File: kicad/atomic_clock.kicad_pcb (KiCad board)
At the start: 2 copper layers, 282.7 x 43 mm, 88 parts, among them J1 Conn_02x05_Top_Bottom, J10 Conn_02x05_Top_Bottom, J11 Conn_02x05_Top_Bottom, J12 USB_B_Micro 10118194-0001LF, J13 ARM_JTAG_SWD_10 3220-10-0100-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, J14 Conn_01x03_Female, J2 Conn_02x05_Top_Bottom, J3 Conn_02x05_Top_Bottom, J4 Conn_02x05_Top_Bottom, J5 USB_B_Micro 1051330001, J6 Conn_02x05_Top_Bottom, J7 Conn_02x05_Top_Bottom, J8 Conn_02x05_Top_Bottom, J9 Conn_02x05_Top_Bottom, Q1 Q_Dual_PMOS, Q2 Q_Dual_PMOS, SW1 SW_Push, U1 D198K, U10 ATSAMDA1E16B-A, U11 D198K, U12 D198K, U13 D198K, U14 D198K, U15 D198K, U16 MAX7221xWG, U17 D198K, U18 D198K, U19 D198K, U2 D198K, U20 NCP1117LPST33T3G, U21 mems_osc_st1630, U22 DHT20, U23 DCF77, U24 MCP73831-2-OT, U25 TXB0101, U3 D198K, U4 D198K, U5 MAX7221xWG, U6 D198K, U7 D198K, U8 D198K, U9 D198K

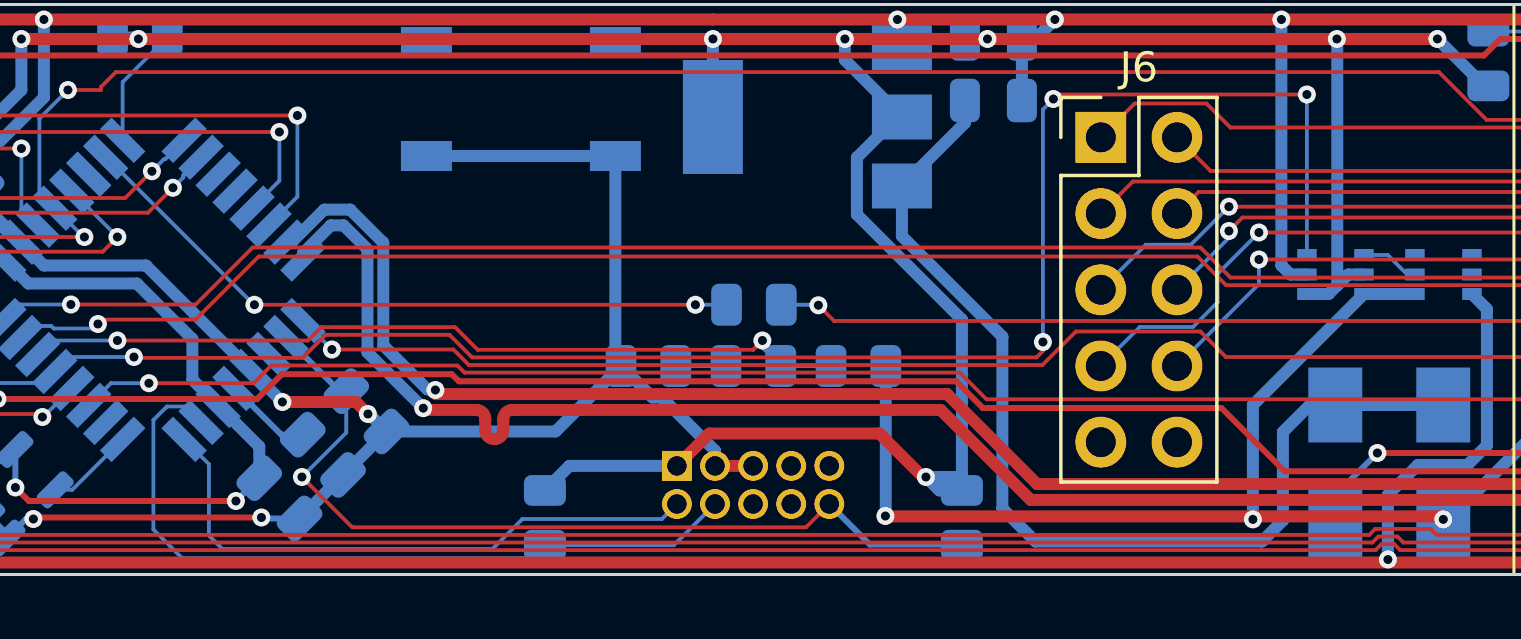
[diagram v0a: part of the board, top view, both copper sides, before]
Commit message: Widen debug connector footprint
The actual header is 12.70mm wide.
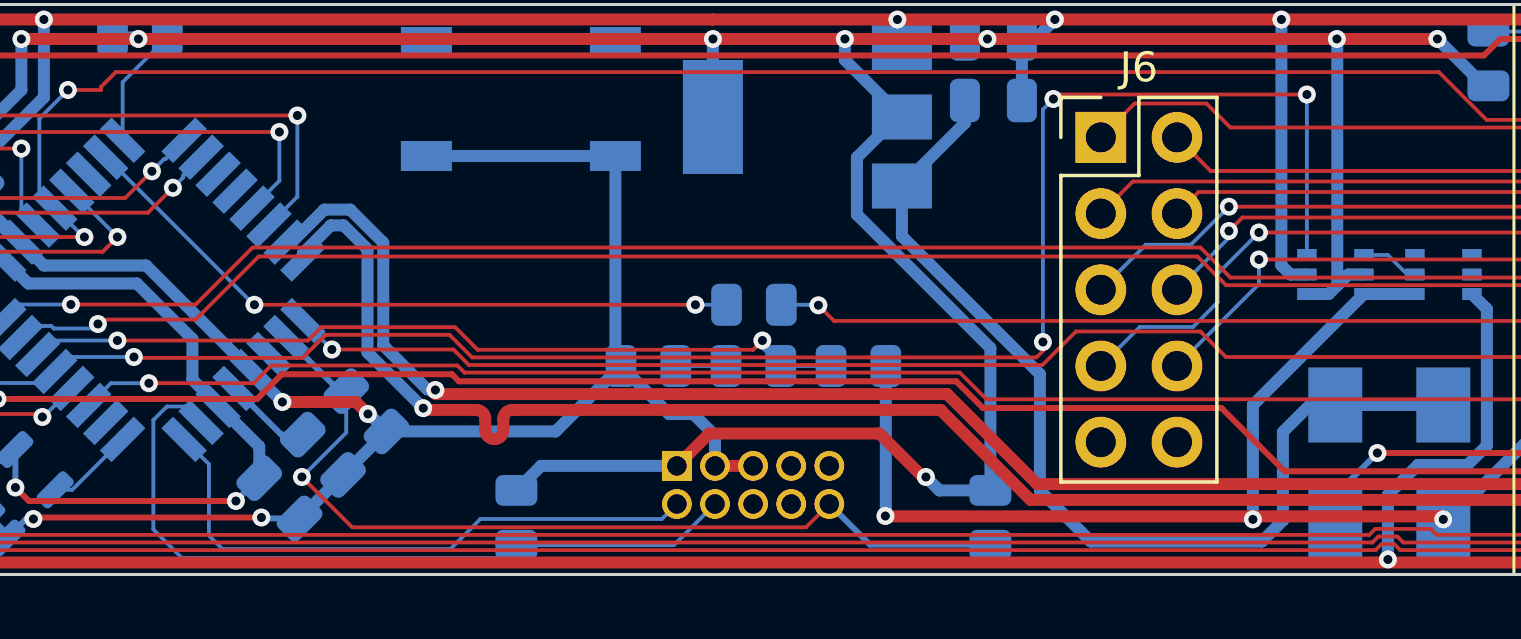
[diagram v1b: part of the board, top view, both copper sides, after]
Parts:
- moved R2 0.95 mm to (116.3, 123.8)
- moved R3 0.95 mm to (132.1, 123.8)
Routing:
- net /3.3V: track 142.9 -> 144.0 mm
- net /NCP_IN: track 34.6 -> 33.5 mm
- net Net-(C6-Pad1): track 29.8 -> 30.8 mm

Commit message: Start routing v2
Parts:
- removed D5, D6, D9: Diode S1M-13-F, Diode_SMD:D_SMA
- removed the REF** at (27.7, 96.0)
- removed the REF** at (300.7, 120.0)
- removed the REF** at (27.7, 120.0)
- removed the REF** at (300.7, 96.0)
- added J15: Conn_01x03_Female, Connector_PinSocket_2.54mm:PinSocket_1x03_P2.54mm_Vertical, B.Cu at (65.6, 116.2)
- added J16: Conn_01x03_Male, Connector_PinHeader_2.54mm:PinHeader_1x03_P2.54mm_Vertical, F.Cu at (118.4, 121.2)
- added RV1: 50K, Potentiometer_SMD:Potentiometer_Bourns_TC33X_Vertical, B.Cu at (67.8, 110.4)
- added SW2: SW_Push, Button_Switch_SMD:SW_SPST_TL3342, B.Cu at (107.8, 121.7)
- BT1: moved to F.Cu
- D8: value Diode S1M-13-F -> Schottky NSR05T40; footprint Diode_SMD:D_SMA -> Diode_SMD:D_SOD-523
- J14: value Conn_01x03_Female -> Conn_01x02_Male; footprint Connector_PinSocket_2.54mm:PinSocket_1x03_P2.54mm_Vertical -> Connector_PinHeader_2.54mm:PinHeader_1x02_P2.54mm_Vertical
- R5: value 10K -> 10M
- moved U22 191.4 mm to (272.0, 120.2), turned to 0 degrees
- moved C8 189.9 mm to (271.2, 123.8), turned to -90 degrees
- moved C7 186.2 mm to (87.6, 108.2), turned to 180 degrees
- moved R4 186.1 mm to (87.6, 124.1), turned to 180 degrees
- moved U16 185.5 mm to (95.3, 116.2)
- moved J5 145.8 mm to (27.8, 117.7)
- moved J12 136.4 mm to (27.8, 122.9)
- moved J14 126.2 mm to (223.7, 113.6), turned to 0 degrees
- moved D8 93.6 mm to (54.4, 109.6), turned to 180 degrees
- moved R10 91.0 mm to (36.9, 124.6), turned to 0 degrees
- moved R3 87.8 mm to (44.3, 124.6), turned to 0 degrees
- moved Q2 86.4 mm to (60.8, 118.5)
- moved U25 86.4 mm to (57.2, 118.5)
- moved R11 84.8 mm to (39.6, 123.8), turned to 90 degrees
- moved R12 79.3 mm to (41.5, 123.8), turned to -90 degrees
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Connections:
- net Net-(C6-Pad1) renamed /~{RESET}
- C10 pad 2: Net-(BT1-Pad1) -> Net-(C10-Pad2)
- J12 pad 1: Net-(D5-Pad2) -> /USB_PWR
- J14 pad 1: GND -> Net-(BT1-Pad1)
- J14 pad 2: /UART_RX -> Net-(C10-Pad2)
- J5 pad 1: Net-(D6-Pad2) -> /USB_PWR
- Q2 pad 3: (no net) -> /NCP_IN
- Q2 pad 4: (no net) -> Net-(C10-Pad2)
- Q2 pad 5: (no net) -> GND
- R1 pad 2: /5V -> /I_SET
- R4 pad 2: /5V -> /I_SET
- R5 pad 1: /3.3V -> /5V
- R5 pad 2: /LDR -> Net-(R5-Pad2)
- R6 pad 1: /LDR_SINK -> Net-(R5-Pad2)
- R6 pad 2: /LDR -> /5V
- U10 pad 19: unconnected-(U10-Pad19) -> /TZ1
- U10 pad 20: unconnected-(U10-Pad20) -> /TZ2
- U10 pad 25: /LDR_SINK -> unconnected-(U10-Pad25)
- U10 pad 3: /LDR -> unconnected-(U10-Pad3)
- U24 pad 3: Net-(BT1-Pad1) -> Net-(C10-Pad2)
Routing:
- net GND: track 470.7 -> 141.5 mm, vias 19 -> 13
- net /~{SS}: track 287.4 -> 0.00 mm, vias 4 -> 0
- net /SCK: track 262.2 -> 0.00 mm, vias 4 -> 0
- net /1s8: track 227.2 -> 0.00 mm, vias 1 -> 0
- net Net-(U16-Pad1): track 241.2 -> 29.4 mm
- net /1s9: track 207.7 -> 0.00 mm, vias 1 -> 0
- net /3.3V_DCF: track 173.5 -> 0.00 mm, vias 1 -> 0
- net /DCF_DATA: track 161.0 -> 0.00 mm, vias 1 -> 0
- net /DCF_PDN: track 158.8 -> 0.00 mm, vias 1 -> 0
- net Net-(BT1-Pad1): track 157.1 -> 0.00 mm, vias 2 -> 0
- net /1A2: track 156.3 -> 0.00 mm, vias 2 -> 0
- net /1B2: track 154.9 -> 0.00 mm, vias 1 -> 0
- net /1DP2: track 151.2 -> 0.00 mm, vias 3 -> 0
- net /1F2: track 150.8 -> 0.00 mm, vias 2 -> 0
- net /1E2: track 148.2 -> 0.00 mm, vias 2 -> 0
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- added copper zone on B.Cu, net GND
- added copper zone on F.Cu, net GND
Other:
- board text added: "Action"
- board text added: "Battery"
- board text added: "LON AMS HEL"
- board text added: "Radio Controlled Clock Syncing to DCF77, Germany v2, October 2022 Erik van Zijst github.com/erikvanzijst/radioclock"
- board text added: "Radio Controlled Clock Syncing to DCF77, Mainflingen, Germany v2, October 2022 Erik van Zijst <erik.van.zijst@gmail.com> github.com/erikvanzijst/radioclock"
- board text added: "Reset"
- board text added: "Timezone"
- board text added: "UART"
- board text removed: "DHT20"
- board text removed: "Radio Controlled Clock Syncing to DCF77, Germany v1.1, June 2022 Erik van Zijst github.com/erikvanzijst/radioclock"
- board text removed: "Radio Controlled Clock Syncing to DCF77, Mainflingen, Germany v1.1, June 2022 Erik van Zijst <erik.van.zijst@gmail.com> github.com/erikvanzijst/radioclock"
- board text removed: "SAMDA1E"
- board text removed: "UART (3.3V)"

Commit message: Route almost all of v2 PCB
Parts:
- moved R4 1.40 mm to (86.2, 124.1)
- moved BT1 0.53 mm to (212.6, 121.9)
- moved C8 0.52 mm to (271.0, 124.3), turned to 180 degrees
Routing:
- net Net-(U10-Pad18): track 0.00 -> 249.1 mm, vias 0 -> 2
- net Net-(U10-Pad17): track 0.00 -> 241.9 mm, vias 0 -> 2
- net Net-(C10-Pad2): track 2.11 -> 216.6 mm, vias 0 -> 3
- net /1s13: track 0.00 -> 205.7 mm, vias 0 -> 1
- net /1s11: track 0.00 -> 199.3 mm, vias 0 -> 1
- net /1s12: track 0.00 -> 199.2 mm, vias 0 -> 1
- net /1s14: track 0.00 -> 197.9 mm, vias 0 -> 1
- net /1s15: track 0.00 -> 195.6 mm, vias 0 -> 1
- net /1s10: track 0.00 -> 195.2 mm, vias 0 -> 1
- net /1B2: track 0.00 -> 151.2 mm, vias 0 -> 1
- net /1F2: track 0.00 -> 148.2 mm, vias 0 -> 3
- net /1A2: track 0.00 -> 147.9 mm, vias 0 -> 1
- net /1DP2: track 0.00 -> 147.6 mm, vias 0 -> 2
- net /1D2: track 0.00 -> 145.8 mm, vias 0 -> 4
- net /1E2: track 0.00 -> 142.7 mm, vias 0 -> 2
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
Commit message: Completed place and route of v2
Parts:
- removed R9: 10K, Resistor_SMD:R_0805_2012Metric
- J16: moved to B.Cu
- turned J16 to -90 degrees
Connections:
- J16 pad 2: /3.3V -> /PERIPHERAL_PWR
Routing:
- net /PERIPHERAL_PWR: track 4.12 -> 255.1 mm, vias 0 -> 3
- net /DCF_PDN: track 0.00 -> 220.5 mm, vias 0 -> 2
- net /DCF_DATA: track 0.00 -> 219.3 mm, vias 0 -> 2
- net /3.3V_DCF: track 0.00 -> 210.4 mm, vias 0 -> 2
- net Net-(R5-Pad2): track 0.00 -> 89.7 mm, vias 0 -> 1
- net /3.3V: track 137.5 -> 63.0 mm, vias 9 -> 7
- net /~{RESET}: track 40.4 -> 88.1 mm, vias 2 -> 3
- net /SWITCH: track 100.6 -> 79.8 mm
- net GND: track 215.9 -> 231.5 mm, vias 19 -> 47
- net /1B2: track 151.2 -> 150.1 mm
- net /~{SS}: track 57.0 -> 56.0 mm
- net Net-(U10-Pad18): track 249.1 -> 248.1 mm
- net Net-(U10-Pad17): track 241.9 -> 241.3 mm
- net /~{DCF_CTL}: track 4.33 -> 4.87 mm
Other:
- board text added: "SAMDA1E"

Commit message: First stab at acrylic glass enclosure
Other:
- board size 282.7 x 43 mm -> 345.2 x 135 mm
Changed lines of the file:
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@@
     (pad_to_mask_clearance 0)
     (aux_axis_origin 22.733 106.674)
-    (grid_origin 22.833 106.674)
+    (grid_origin 308.533 162.224)
     (pcbplotparams
       (layerselection 0x00010fc_ffffffff)
@@
   (gr_line (start 149.533 106.724) (end 149.533 125.624) (layer "F.SilkS") (width 0.1))
   (gr_circle (center 200.783 116.174) (end 192.783 116.174) (layer "F.SilkS") (width 0.3) (fill none))
+  (gr_line (start 19.833 187.224) (end 19.833 162.224) (layer "Edge.Cuts") (width 0.1))
   (gr_rect (start 22.833 101.6738) (end 149.633 82.6738) (layer "Edge.Cuts") (width 0.1) (fill none))
+  (gr_line (start 19.833 135.174) (end 308.533 135.174) (layer "Edge.Cuts") (width 0.1))
+  (gr_line (start 308.533 187.224) (end 19.833 187.224) (layer "Edge.Cuts") (width 0.1))
   (gr_line (start 205.733 124.174) (end 205.733 125.674) (layer "Edge.Cuts") (width 0.1))
+  (gr_line (start 19.833 162.224) (end 308.533 162.224) (layer "Edge.Cuts") (width 0.1))
+  (gr_line (start 19.833 192.674) (end 308.533 192.674) (layer "Edge.Cuts") (width 0.1))
+  (gr_line (start 308.533 187.224) (end 308.533 162.224) (layer "Edge.Cuts") (width 0.1))
+  (gr_line (start 333.283 120.624) (end 333.283 122.124) (layer "Edge.Cuts") (width 0.1))
+  (gr_arc (start 331.283 120.624) (mid 332.283 119.624) (end 333.283 120.624) (layer "Edge.Cuts") (width 0.1))
+  (gr_line (start 19.833 217.674) (end 19.833 192.674) (layer "Edge.Cuts") (width 0.1))
+  (gr_rect (start 311.533 165.224) (end 336.533 184.224) (layer "Edge.Cuts") (width 0.1) (fill none))
   (gr_arc (start 205.733 124.174) (mid 206.733 123.174) (end 207.733 124.174) (layer "Edge.Cuts") (width 0.1))
+  (gr_line (start 19.833 160.174) (end 19.833 135.174) (layer "Edge.Cuts") (width 0.1))
+  (gr_line (start 308.533 160.174) (end 308.533 135.174) (layer "Edge.Cuts") (width 0.1))
   (gr_line (start 305.533 125.674) (end 305.533 106.674) (layer "Edge.Cuts") (width 0.1))
   (gr_line (start 22.833 125.674) (end 22.833 106.674) (layer "Edge.Cuts") (width 0.1))
   (gr_line (start 207.733 124.174) (end 207.733 125.674) (layer "Edge.Cuts") (width 0.1))
+  (gr_line (start 308.533 217.674) (end 19.833 217.674) (layer "Edge.Cuts") (width 0.1))
   (gr_line (start 205.733 125.674) (end 22.833 125.674) (layer "Edge.Cuts") (width 0.1))
+  (gr_line (start 308.533 217.674) (end 308.533 192.674) (layer "Edge.Cuts") (width 0.1))
   (gr_line (start 207.733 125.674) (end 305.533 125.674) (layer "Edge.Cuts") (width 0.1))
   (gr_rect (start 216.833 101.6738) (end 305.533 82.6738) (layer "Edge.Cuts") (width 0.1) (fill none))
+  (gr_line (start 331.283 120.624) (end 331.283 122.124) (layer "Edge.Cuts") (width 0.1))
   (gr_line (start 22.833 106.674) (end 305.533 106.674) (layer "Edge.Cuts") (width 0.1))
+  (gr_rect (start -8.617 165.174) (end 16.383 184.174) (layer "Edge.Cuts") (width 0.1) (fill none))
+  (gr_line (start 308.533 160.174) (end 19.833 160.174) (layer "Edge.Cuts") (width 0.1))
   (gr_rect (start 19.833 130.6738) (end 308.533 77.6738) (layer "User.1") (width 0.1) (fill none))
   (gr_text "CP1654\nCoin cell" (at 212.883 116.174) (layer "B.SilkS")
@@
   )
   (dimension (type aligned) (layer "User.1")
-    (pts (xy 308.533 130.6738) (xy 19.833 130.6738))
+    (pts (xy 305.533 125.674) (xy 22.833 125.674))
     (height -6.7)
-    (gr_text "288.7000 mm" (at 164.183 135.5738) (layer "User.1")
+    (gr_text "282.7000 mm" (at 164.183 130.574) (layer "User.1")
       (effects (font (size 1.5 1.5) (thickness 0.3)))
     )
@@
         (xy 258.833 125.774)
         (xy 258.833 109.674)
-        (xy 258.833 109.674)
       )

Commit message: Drew the enclosure in PCBNew
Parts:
- removed BT1: Varta CP1654 A3, local_footprints:Battery_pads
- removed C1, C4, C6, C7, C8: 100nF 885012207016, Capacitor_SMD:C_0805_2012Metric
- removed C10, C9: 4.7uF CL21A475KPFNNNE, Capacitor_SMD:C_0805_2012Metric
- removed C11, C2, C3: 10uF CL21A106KPFNNNF, Capacitor_SMD:C_0805_2012Metric
- removed C5: 1uF 885012207051, Capacitor_SMD:C_0805_2012Metric
- removed D1, D2, D3, D4: LED LTL-1224A, local_footprints:LED_D2.0mm_W4.8mm_H2.5mm_FlatTop
- removed D10, D7: LED HSMS-C150, LED_SMD:LED_1206_3216Metric_Pad1.42x1.75mm_HandSolder
- removed D8: Schottky NSR05T40, Diode_SMD:D_SOD-523
- removed J1, J10, J11, J2, J3, J4, J6, J7, J8, J9: Conn_02x05_Top_Bottom, Connector_PinHeader_2.54mm:PinHeader_2x05_P2.54mm_Vertical
- removed J12: USB_B_Micro 10118194-0001LF, Connector_USB:USB_Micro-B_Amphenol_10118194_Horizontal
- removed J13: ARM_JTAG_SWD_10 3220-10-0100-00, local_footprints:sam_swd_header
- removed J14: Conn_01x02_Male, Connector_PinHeader_2.54mm:PinHeader_1x02_P2.54mm_Vertical
- removed J15: Conn_01x03_Female, Connector_PinSocket_2.54mm:PinSocket_1x03_P2.54mm_Vertical
- removed J16: Conn_01x03_Male, Connector_PinHeader_2.54mm:PinHeader_1x03_P2.54mm_Vertical
- removed J5: USB_B_Micro 1051330001, Connector_USB:USB_Micro-B_Molex-105133-0001
- removed Q1, Q2: Q_Dual_PMOS, Package_TO_SOT_SMD:SOT-363_SC-70-6
- removed R1, R10, R11, R12, R13, R14, R15, R3, R4, R7: 10K, Resistor_SMD:R_0805_2012Metric
- removed R16: 220R, Resistor_SMD:R_0805_2012Metric
- removed R2: 1K, Resistor_SMD:R_0805_2012Metric
- removed R5: 10M, Resistor_SMD:R_0805_2012Metric
- removed R6: LDR NSL-19M51, OptoDevice:R_LDR_4.9x4.2mm_P2.54mm_Vertical
- removed R8: 470R, Resistor_SMD:R_0805_2012Metric
- removed REF** (x4): MountingHole_2.2mm_M2, MountingHole:MountingHole_2.2mm_M2
- removed RV1: 50K, Potentiometer_SMD:Potentiometer_Bourns_TC33X_Vertical
- removed SW1, SW2: SW_Push, Button_Switch_SMD:SW_SPST_TL3342
- removed U1, U11, U12, U13, U14, U15, U17, U18, U19, U2, U3, U4, U6, U7, U8, U9: D198K, Display_7Segment:D1X8K
- removed U10: ATSAMDA1E16B-A, Package_QFP:TQFP-32_7x7mm_P0.8mm
- removed U16, U5: MAX7221xWG, Package_SO:SOIC-24W_7.5x15.4mm_P1.27mm
- removed U20: NCP1117LPST33T3G, Package_TO_SOT_SMD:SOT-223
- removed U21: mems_osc_st1630, Package_TO_SOT_SMD:SOT-23-5
- removed U22: DHT20, local_footprints:DHT20
- removed U23: DCF77, local_footprints:DCF77 receiver module
- removed U24: MCP73831-2-OT, Package_TO_SOT_SMD:SOT-23-5
- removed U25: TXB0101, Package_TO_SOT_SMD:SOT-363_SC-70-6
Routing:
- net /5V: track 261.0 -> 0.00 mm, vias 5 -> 0
- net /PERIPHERAL_PWR: track 255.1 -> 0.00 mm, vias 3 -> 0
- net Net-(U10-Pad18): track 248.1 -> 0.00 mm, vias 2 -> 0
- net Net-(U10-Pad17): track 241.3 -> 0.00 mm, vias 2 -> 0
- net GND: track 231.5 -> 0.00 mm, vias 47 -> 0
- net /DCF_PDN: track 220.5 -> 0.00 mm, vias 2 -> 0
- net /DCF_DATA: track 219.3 -> 0.00 mm, vias 2 -> 0
- net Net-(C10-Pad2): track 216.9 -> 0.00 mm, vias 3 -> 0
- net /3.3V_DCF: track 210.4 -> 0.00 mm, vias 2 -> 0
- net /1s13: track 205.9 -> 0.00 mm, vias 1 -> 0
- net /1s11: track 199.3 -> 0.00 mm, vias 1 -> 0
- net /1s12: track 199.2 -> 0.00 mm, vias 1 -> 0
- net /1s14: track 197.9 -> 0.00 mm, vias 1 -> 0
- net /1s15: track 195.6 -> 0.00 mm, vias 1 -> 0
- net /1s10: track 195.0 -> 0.00 mm, vias 1 -> 0
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- removed copper zone on B.Cu, net GND
- removed copper zone on F.Cu, net GND
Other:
- board size 345.2 x 135 mm -> 290.7 x 72.8 mm
- board text removed: "25mA @ 4.2v Charge current"
- board text removed: "Action"
- board text removed: "Batt full Charging"
- board text removed: "Battery"
- board text removed: "CP1654 Coin cell"
- board text removed: "Ferrite core antenna"
- board text removed: "GND"
- board text removed: "JLCJLCJLCJLC"
- board text removed: "LON AMS HEL"
- board text removed: "MAS DAEV6180B1COB.005 Time signal receiver module"
- board text removed: "MAX7221"
- board text removed: "PCB A"
- board text removed: "PCB B"
- board text removed: "PCB C"
- board text removed: "RX"
- board text removed: "Radio Controlled Clock Syncing to DCF77, Germany v2, October 2022 Erik van Zijst github.com/erikvanzijst/radioclock"
- board text removed: "Radio Controlled Clock Syncing to DCF77, Mainflingen, Germany v2, October 2022 Erik van Zijst <erik.van.zijst@gmail.com> github.com/erikvanzijst/radioclock"
- board text removed: "Rechargeable LiPo only!"
- board text removed: "Reset"
- board text removed: "SAMDA1E"
- board text removed: "TOP"
- board text removed: "TX"
- board text removed: "Timezone"
- board text removed: "UART"
- board text removed: "◯ ◉"
